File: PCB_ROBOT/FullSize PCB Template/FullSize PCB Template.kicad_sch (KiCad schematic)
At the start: 4 parts

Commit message: REV 2 - metadata update
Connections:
- net GND: now reaches H3.1
- net GND: now also H1.1, H2.1, H4.1
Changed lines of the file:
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@@
 		(company "FabRice Team - Campus Fab")
+	)
+	(junction
+		(at 49.53 86.36)
+		(diameter 0)
+		(color 0 0 0 0)
+	)
+	(junction
+		(at 49.53 102.87)
+		(diameter 0)
+		(color 0 0 0 0)
+	)
+	(junction
+		(at 49.53 95.25)
+		(diameter 0)
+		(color 0 0 0 0)
+	)
+	(wire
+		(pts
+			(xy 49.53 95.25) (xy 49.53 102.87)
+		)
+		(stroke
+			(width 0)
+			(type default)
+		)
+	)
+	(wire
+		(pts
+			(xy 49.53 86.36) (xy 49.53 95.25)
+		)
+		(stroke
+			(width 0)
+			(type default)
+		)
+	)
+	(wire
+		(pts
+			(xy 49.53 77.47) (xy 49.53 86.36)
+		)
+		(stroke
+			(width 0)
+			(type default)
+		)
+	)
+	(wire
+		(pts
+			(xy 60.96 102.87) (xy 49.53 102.87)
+		)
+		(stroke
+			(width 0)
+			(type default)
+		)
+	)
+	(wire
+		(pts
+			(xy 60.96 77.47) (xy 49.53 77.47)
+		)
+		(stroke
+			(width 0)
+			(type default)
+		)
+	)
+	(wire
+		(pts
+			(xy 60.96 86.36) (xy 49.53 86.36)
+		)
+		(stroke
+			(width 0)
+			(type default)
+		)
+	)
+	(wire
+		(pts
+			(xy 60.96 95.25) (xy 49.53 95.25)
+		)
+		(stroke
+			(width 0)
+			(type default)
+		)
+	)
+	(wire
+		(pts
+			(xy 49.53 102.87) (xy 49.53 107.95)
+		)
+		(stroke
+			(width 0)
+			(type default)
+		)
 	)
 	(symbol
@@
 		)
 		(instances
-			(project "LAYER_0"
+			(project "FullSize PCB Template"
 				(path "/4dcad6ef-b86b-4983-8ea3-3e85f09ba8be"
 					(reference "H3")
@@
 		)
 		(instances
-			(project "LAYER_0"
+			(project "FullSize PCB Template"
 				(path "/4dcad6ef-b86b-4983-8ea3-3e85f09ba8be"
 					(reference "H1")
@@
 		)
 		(instances
-			(project "LAYER_0"
+			(project "FullSize PCB Template"
 				(path "/4dcad6ef-b86b-4983-8ea3-3e85f09ba8be"
 					(reference "H4")
@@
 		)
 		(instances
-			(project "LAYER_0"
+			(project "FullSize PCB Template"
 				(path "/4dcad6ef-b86b-4983-8ea3-3e85f09ba8be"
 					(reference "H2")
 					(unit 1)
 				)
+			)
+		)
+	)
+	(symbol
+		(lib_id "power:GND")
+		(at 49.53 107.95 0)
+		(unit 1)
+		(exclude_from_sim no)
+		(in_bom yes)
+		(on_board yes)
+		(dnp no)
+		(fields_autoplaced yes)
+		(property "Reference" "#PWR01"
+			(at 49.53 114.3 0)
+			(effects
+				(font
+					(size 1.27 1.27)
+				)
+				(hide yes)
+			)
+		)
+		(property "Value" "GND"
+			(at 49.53 113.03 0)
+			(effects
+				(font
+					(size 1.27 1.27)
+				)
+			)
+		)
+		(property "Footprint" ""
+			(at 49.53 107.95 0)
+			(effects
+				(font
+					(size 1.27 1.27)
+				)
+				(hide yes)
+			)
+		)
+		(property "Datasheet" ""
+			(at 49.53 107.95 0)
+			(effects
+				(font
+					(size 1.27 1.27)
+				)
+				(hide yes)
+			)
+		)
+		(property "Description" "Power symbol creates a global label with name \"GND\" , ground"
+			(at 49.53 107.95 0)
+			(effects
+				(font
+					(size 1.27 1.27)
+				)
+				(hide yes)
+			)
+		)
+		(pin "1"
+		)
+		(instances
+			(project "FullSize PCB Template"
+				(path "/4dcad6ef-b86b-4983-8ea3-3e85f09ba8be"
+					(reference "#PWR01")
+					(unit 1)
+				)

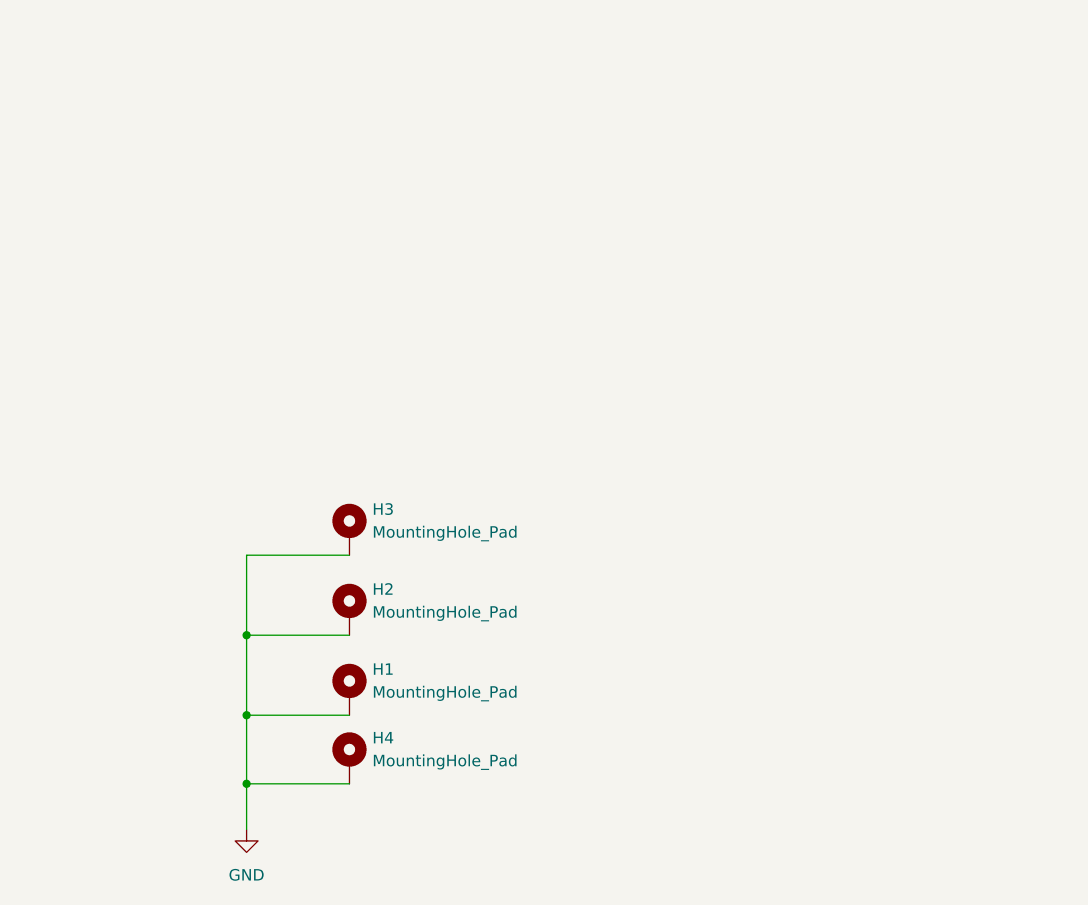
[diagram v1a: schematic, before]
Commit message: FullSize Template Revision
Adding standard power connector
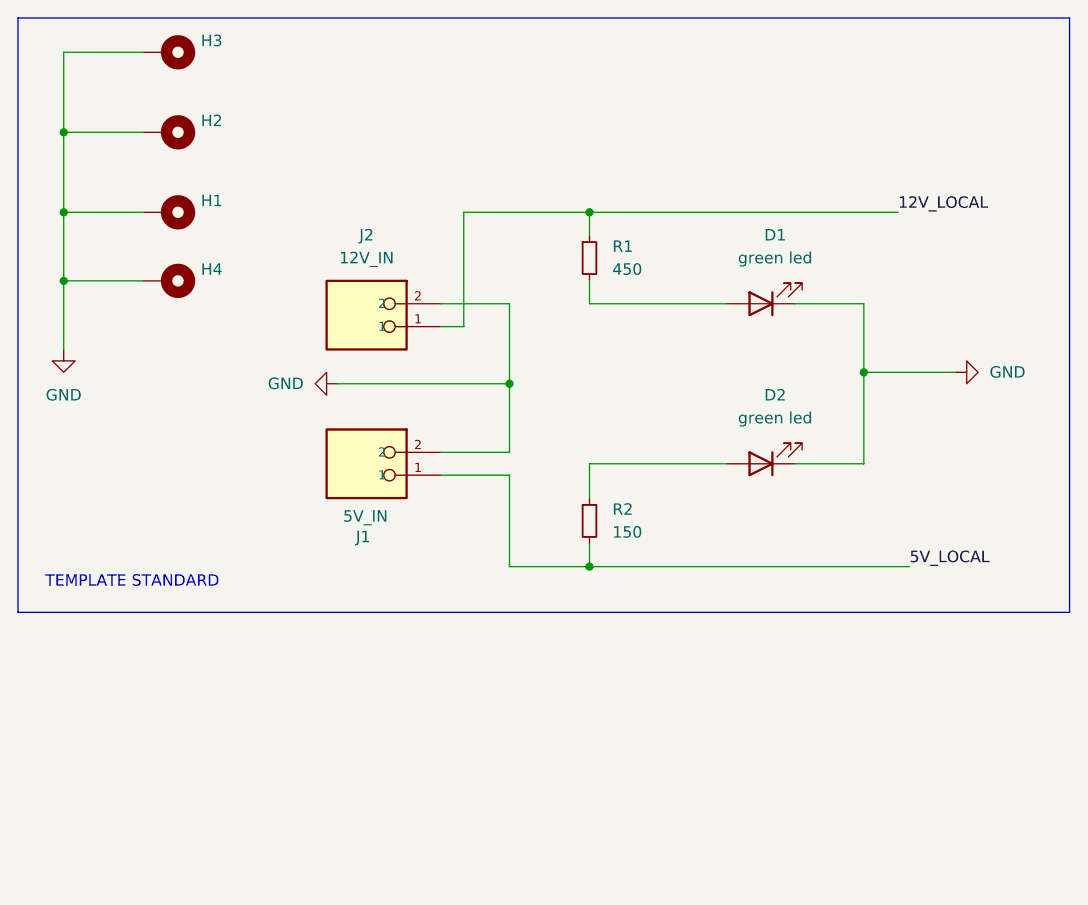
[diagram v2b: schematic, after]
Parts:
- added D1, D2: green led, LED_SMD:LED_0805_2012Metric, symbol Device:LED
- added J1: 5V_IN, Footprints:PHOENIX_1984963, symbol 1984963:1984963
- added J2: 12V_IN, Footprints:PHOENIX_1984963, symbol 1984963:1984963
- added R1: 450, Resistor_SMD:R_1206_3216Metric, symbol Device:R_Small
- added R2: 150, Resistor_SMD:R_1206_3216Metric, symbol Device:R_Small
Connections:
- net GND: now also D1.1 (K), D2.1 (K), J1.2, J2.2
- new net: D2.2 (A), R2.1
- new net: D1.2 (A), R1.2
- new net 12V_LOCAL: J2.1, R1.1
- new net 5V_LOCAL: J1.1, R2.2
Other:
- note added: "TEMPLATE STANDARD"
- moved on the sheet: H1, H2, H3, H4
